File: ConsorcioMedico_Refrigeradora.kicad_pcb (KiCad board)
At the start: 2 copper layers, 260 x 70 mm, 149 parts, among them J1 BatteryHolder, J10 AC, J11 Digital, J12 Light, J13 Light, J14 Compress, J15 Resistor, J16 Analog, J18 Resistor, J19 AC, J2 USART, J3 USART, J4 SWD, J5 Evap_fan, J8 Evap_fan, J9 Compress, K1 HF46F-G/012-HS1T, K2 AZ2150-1A-12DEF, K3 HF46F-G/012-HS1T, K4 HF46F-G/012-HS1T, Q1 MMBT3904, Q2 MMBT3904, Q3 MMBT3904, Q4 MMBT3904, Q5 BSS806, Q6 BSS806, Q7 BSS806, Q8 BSS806, Q9 BSS806, U1 STM32F411RETx, U2 AP63205WU, U3 LDL1117, U4 INA350, U5 INA350, U6 LTV-357T, U7 LTV-357T, U9 HLK-PMx, Y1 8Mhz, Y2 32.768khz/12.5pF

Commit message: SCH: Se añadieron pads en el capacitor de la fuente principal en caso de que el de tipo SMD no dure mucho. PCB: Se enrutó, se colocaron los planos GND, se acomodó la serigrafía
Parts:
- added J6: Screw_Terminal_01x01, 1-Pad:Pad_0.7mm_1.3mm, F.Cu at (81.0, 88.5)
- added J7: Screw_Terminal_01x01, 1-Pad:Pad_0.7mm_1.3mm, F.Cu at (77.1, 88.5)
- moved J4 12.5 mm to (35.2, 108.1), turned to -90 degrees
- moved C1 7.48 mm to (46.2, 110.7), turned to 0 degrees
- moved C29 1.60 mm to (78.8, 88.5), turned to 180 degrees
- moved Q5 1.55 mm to (199.5, 87.7)
- moved R33 1.51 mm to (196.5, 87.7)
- moved R31 1.47 mm to (194.5, 87.7)
- moved J12 1.44 mm to (176.6, 66.1)
- moved J9 1.30 mm to (259.6, 66.2)
- moved J5 1.25 mm to (208.1, 65.3)
- moved J15 1.23 mm to (196.6, 66.1)
- moved Q7 0.86 mm to (159.0, 86.3)
- moved C19 0.80 mm to (84.4, 106.9), turned to -90 degrees
- moved J13 0.80 mm to (176.6, 75.0)
- moved R37 0.80 mm to (154.0, 86.3)
- moved R40 0.80 mm to (156.0, 86.3)
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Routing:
- net GND: track 0.00 -> 464.6 mm, vias 0 -> 67
- net +3.3V: track 169.9 -> 495.2 mm, vias 7 -> 51
- net +12V: track 179.9 -> 409.1 mm, vias 5 -> 9
- net SWDIO: track 0.00 -> 58.2 mm, vias 0 -> 2
- net SWCLK: track 0.00 -> 55.1 mm, vias 0 -> 1
- net +BATT: track 3.04 -> 51.3 mm, vias 0 -> 2
- net SWO: track 0.00 -> 46.8 mm, vias 0 -> 2
- net RESET: track 0.00 -> 44.3 mm, vias 0 -> 4
- net Button_Cooling: track 178.5 -> 186.9 mm
- net Net-(Q8-G): track 0.00 -> 4.08 mm
- net DIG3: track 31.9 -> 34.8 mm
- net Relay_Fan: track 143.6 -> 141.0 mm
- net Net-(D9-PadA): track 0.00 -> 2.26 mm
- net Net-(Q2-B): track 0.00 -> 2.07 mm
- net LED_Status: track 29.9 -> 31.7 mm
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- added copper zone on B.Cu, net +3.3V
- added copper zone on F.Cu, net +3.3V
- added copper zone on B.Cu, net GND
- added copper zone on F.Cu, net GND
- added copper zone on F.Cu, net Net-(J12-Pin_1)
- added copper zone on F.Cu, net Net-(J13-Pin_1)
- added copper zone on F.Cu, net Net-(J14-Pin_1)
- added copper zone on F.Cu, net Net-(J15-Pin_1)
- added copper zone on F.Cu, net Net-(J18-Pin_1)
- added copper zone on F.Cu, net Net-(J5-Pin_1)
- added copper zone on F.Cu, net Net-(J8-Pin_1)
- added copper zone on F.Cu, net Net-(J9-Pin_1)
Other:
- outline, holes or cut-outs redrawn

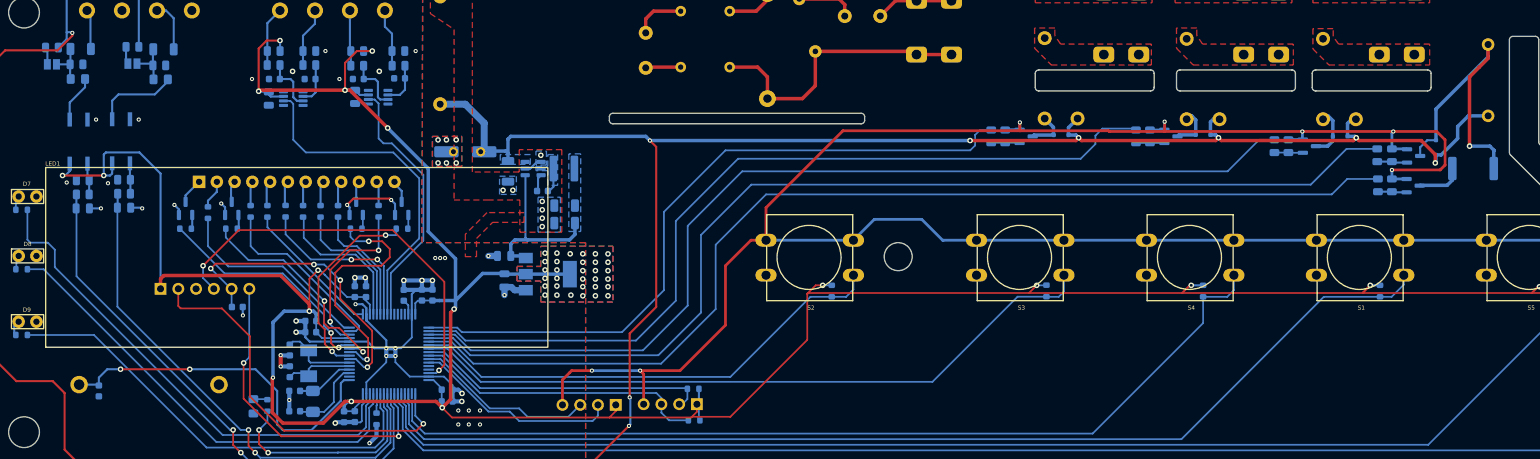
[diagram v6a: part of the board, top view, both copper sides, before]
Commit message: SCH: Se modicaron algunos valores y comentarios del sch. PCB: Posiblemente debido a jlcpcb. JLCPCB: Se asigna el código para la soldura
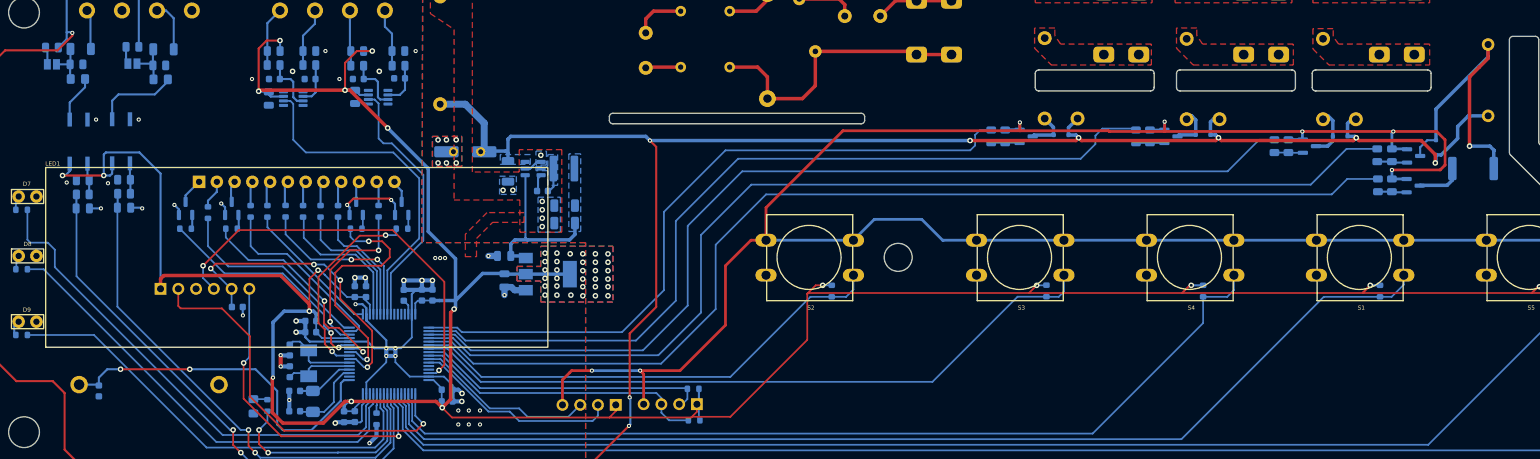
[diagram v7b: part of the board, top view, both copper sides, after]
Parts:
- R1: value 1000 -> 1k
- RV1: value FNR6045S680 -> RM10D561KD24E100
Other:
- outline, holes or cut-outs redrawn

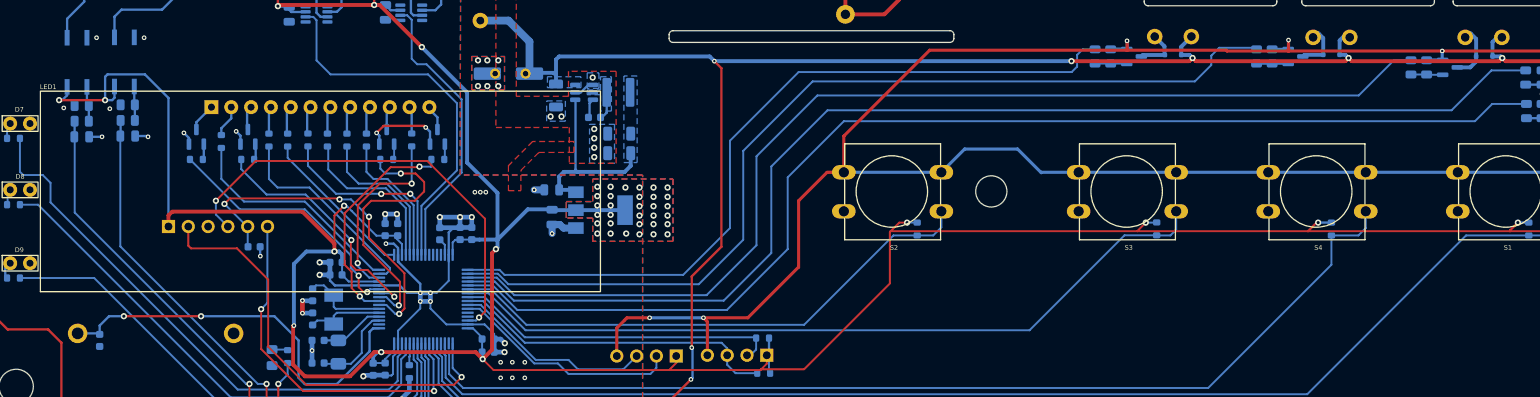
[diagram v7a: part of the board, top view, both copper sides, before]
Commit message: SCH: Se arregló la posición de los pulsadores, se agrega buzzer, PCB: Se revisan los componentes y se agrega serigrafía. JLCPCB: Actualizado
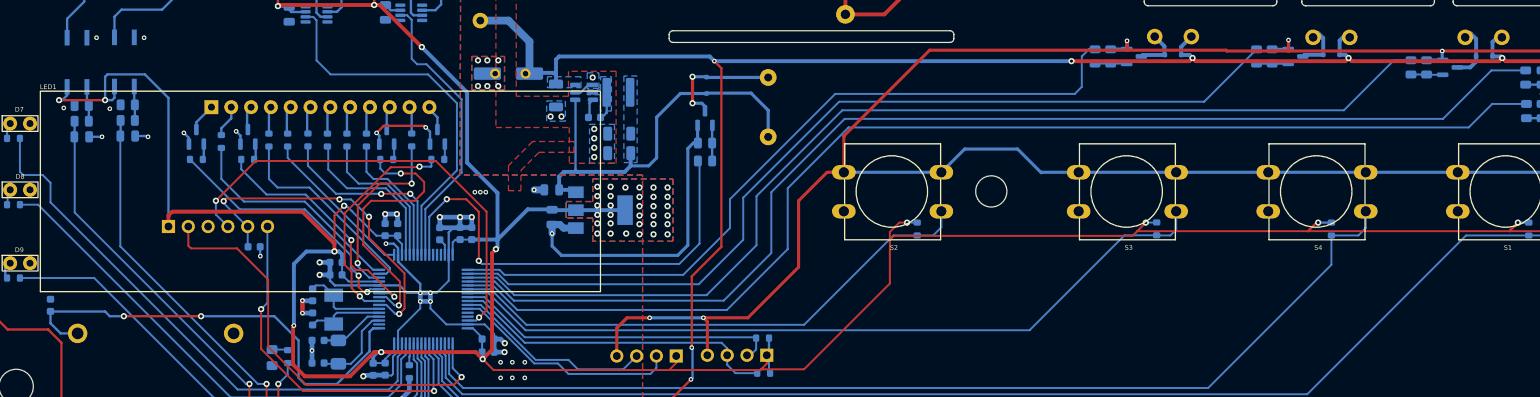
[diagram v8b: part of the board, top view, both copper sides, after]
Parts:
- added D2: 1N4148WS, Diode_SMD:D_SOD-323, B.Cu at (104.2, 90.0)
- added Q11: BSS806, Package_TO_SOT_SMD:SOT-23, B.Cu at (104.0, 94.2)
- added R56: 220R, 1-Resistor:R_0805_2012Metric, B.Cu at (104.0, 99.7)
- added R57: 10K, 1-Resistor:R_0805_2012Metric, B.Cu at (104.0, 97.4)
- added SG2: F_TMB, 1-Buzzer-and-Speaker-Eagle:F_TMB, B.Cu at (112.1, 92.8)
- moved C12 7.74 mm to (20.1, 118.2), turned to 90 degrees
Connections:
- R15 pad 1: Button_Buzzer -> Button_Down
- R16 pad 1: Button_Touch -> Button_Buzzer
- R17 pad 1: Button_Up -> Button_Touch
- R18 pad 1: Button_Down -> Button_Up
- S1 pad 1: Button_Buzzer -> Button_Down
- S2 pad 1: Button_Touch -> Button_Buzzer
- S3 pad 1: Button_Up -> Button_Touch
- S4 pad 1: Button_Down -> Button_Up
- U1 pad 26: unconnected-(U1-PB0-Pad26) -> Relay_On
- U1 pad 38: Button_Touch -> Button_Buzzer
- U1 pad 39: Button_Up -> Button_Touch
- U1 pad 51: Button_Down -> Button_Up
- U1 pad 52: Button_Buzzer -> Button_Down
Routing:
- net Button_Buzzer: track 158.3 -> 69.8 mm
- net Relay_On: track 0.00 -> 59.4 mm, vias 0 -> 2
- net GND: track 464.6 -> 500.9 mm
- net Button_Up: track 100.5 -> 135.2 mm
- net Button_Touch: track 69.8 -> 100.5 mm
- net +5V: track 24.7 -> 53.6 mm
- net Button_Down: track 135.2 -> 158.3 mm
- net Net-(D2-A): track 0.00 -> 15.5 mm, vias 0 -> 2
- net +BATT: track 51.3 -> 58.8 mm
- net Net-(Q11-G): track 0.00 -> 4.58 mm
- net Relay_Calefac: track 121.7 -> 117.3 mm
- net Relay_Light: track 100.1 -> 97.1 mm
- net Relay_Fan: track 141.0 -> 138.0 mm
- net Relay_Compressor: track 155.4 -> 153.4 mm
- net Relay_Compressor_Save: track 153.4 -> 152.5 mm
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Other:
- board text added: "3.3V"
- board text added: "CLK"
- board text added: "GND"
- board text added: "RST"
- board text added: "RX"
- board text added: "SCL"
- board text added: "SDA"
- board text added: "SWDIO"
- board text added: "SWO"
- board text added: "TX"
